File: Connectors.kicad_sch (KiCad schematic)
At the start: 13 parts

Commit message: Update V0.3
Quashed all the DRC errors! Probably pretty stable now.
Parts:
- CM1, CM2, CM3: footprint (none) -> oresat-proto-card:J-MOLEX-SMPM-073300-003X
- H2, H3: value (none) -> STAND-OFFTIGHT; footprint (none) -> oresat-proto-card:STAND-OFF-TIGHT
- J1: footprint (none) -> oresat-proto-card:J-SAMTEC-TFM-110-X1-XXX-D-RA
- J2, J3, J4: footprint (none) -> oresat-proto-card:U.FL
- J6: footprint (none) -> oresat-proto-card:J-SAMTEC-TFM-120-X1-XXX-D-RA
- JP10, JP2: footprint (none) -> oresat-proto-card:2X05
- JP9: footprint (none) -> oresat-proto-card:1X10

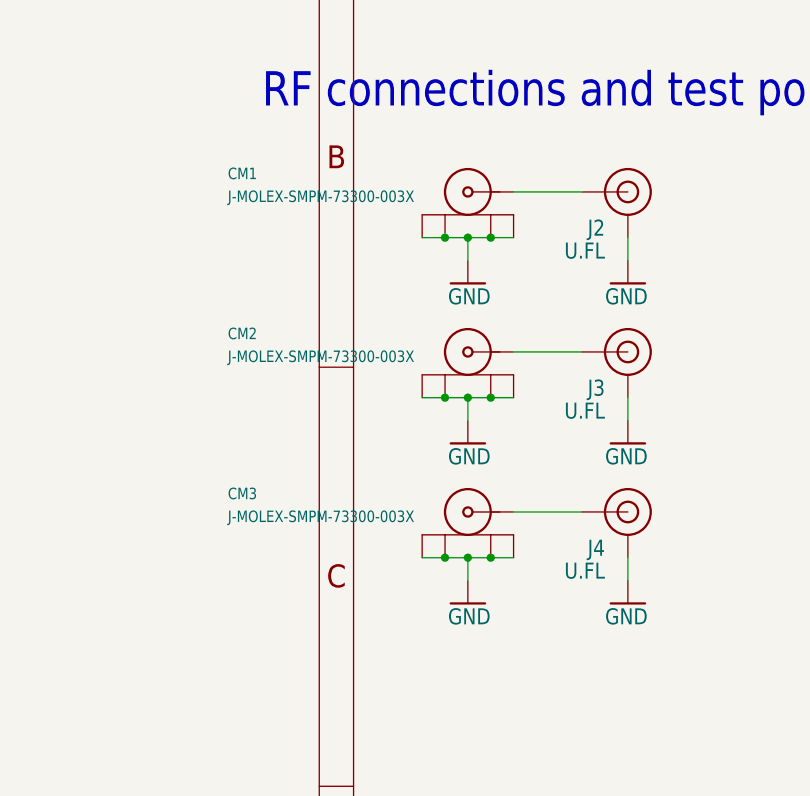
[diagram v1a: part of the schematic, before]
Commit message: V0.4 BOM Updates and Footprint Fixes
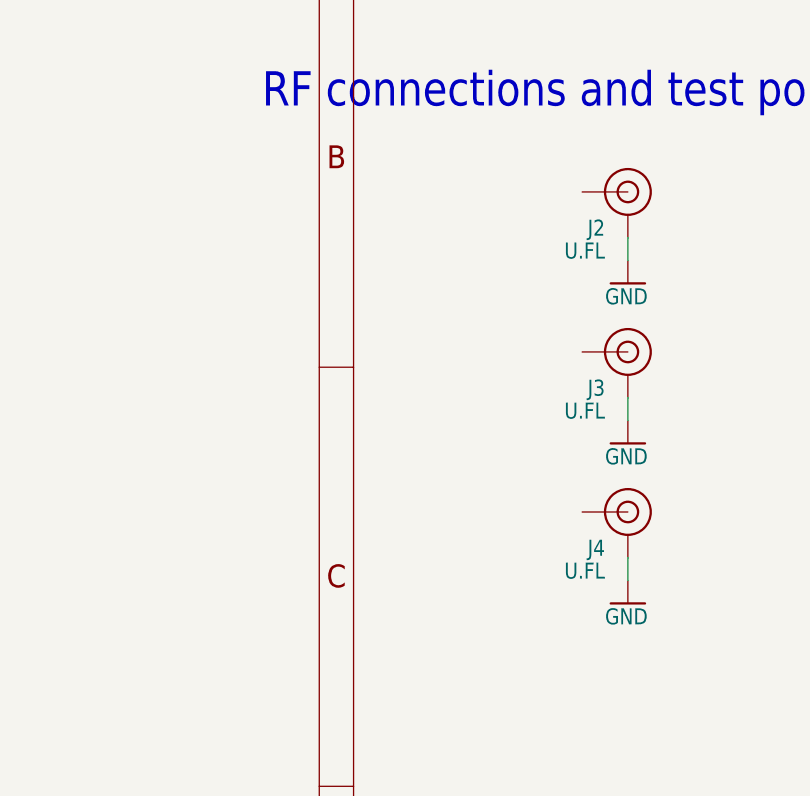
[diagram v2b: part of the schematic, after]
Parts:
- removed CM1, CM2, CM3: (no value), oresat-proto-card:J-MOLEX-SMPM-073300-003X, symbol oresat-proto-card-eagle-import:J-MOLEX-SMPM-73300-003X
- J6: Generic (none) -> N; Manufacturer_Name (none) -> Samtech; Manufacturer_Part_Number (none) -> TFM-120-01-L-D-RA
